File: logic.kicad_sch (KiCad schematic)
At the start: 42 parts, among them J2 TC2030, J5 Conn_01x04_Pin, J8 Conn_01x04, J9 Conn_01x04, SW1 SW_Push, SW2 SW_Push, U2 SN65HVD230, U4 HT753-1, U6 STM32F103C8Tx, Y1 8M

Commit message: schem: run and fix ERC
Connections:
- net GND: now also C6.2, C8.2, C9.2, R7.1
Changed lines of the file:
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@@
+	)
+	(symbol
+		(lib_id "power:GND")
+		(at 96.52 85.09 0)
+		(unit 1)
+		(body_style 1)
+		(exclude_from_sim no)
+		(in_bom yes)
+		(on_board yes)
+		(in_pos_files yes)
+		(dnp no)
+		(fields_autoplaced yes)
+		(property "Reference" "#PWR035"
+			(at 96.52 91.44 0)
+			(hide yes)
+			(show_name no)
+			(do_not_autoplace no)
+			(effects
+				(font
+					(size 1.27 1.27)
+				)
+			)
+		)
+		(property "Value" "GND"
+			(at 96.52 90.17 0)
+			(hide yes)
+			(show_name no)
+			(do_not_autoplace no)
+			(effects
+				(font
+					(size 1.27 1.27)
+				)
+			)
+		)
+		(property "Footprint" ""
+			(at 96.52 85.09 0)
+			(hide yes)
+			(show_name no)
+			(do_not_autoplace no)
+			(effects
+				(font
+					(size 1.27 1.27)
+				)
+			)
+		)
+		(property "Datasheet" ""
+			(at 96.52 85.09 0)
+			(hide yes)
+			(show_name no)
+			(do_not_autoplace no)
+			(effects
+				(font
+					(size 1.27 1.27)
+				)
+			)
+		)
+		(property "Description" "Power symbol creates a global label with name \"GND\" , ground"
+			(at 96.52 85.09 0)
+			(hide yes)
+			(show_name no)
+			(do_not_autoplace no)
+			(effects
+				(font
+					(size 1.27 1.27)
+				)
+			)
+		)
+		(pin "1"
+		)
+		(instances
+			(project "s6tm-detect-psu-1"
+				(path "/c28e80f1-f767-484a-bf96-16c1e8738b05/a8ebaca3-da9e-4a0a-a7e6-414b19783be9"
+					(reference "#PWR035")
+					(unit 1)
+				)
+			)
+		)
 	)
 	(symbol

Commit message: schem: add missing parts to BOM
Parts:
- J8, J9: now in the parts list
- JP4, JP5: now left out of the parts list
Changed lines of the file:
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@@
 		(body_style 1)
 		(exclude_from_sim no)
-		(in_bom no)
+		(in_bom yes)
 		(on_board yes)
 		(in_pos_files yes)
@@
 		(body_style 1)
 		(exclude_from_sim no)
-		(in_bom no)
+		(in_bom yes)
 		(on_board yes)
 		(in_pos_files yes)
@@
 		(body_style 1)
 		(exclude_from_sim no)
-		(in_bom yes)
+		(in_bom no)
 		(on_board yes)
 		(in_pos_files yes)
@@
 		(body_style 1)
 		(exclude_from_sim no)
-		(in_bom yes)
+		(in_bom no)
 		(on_board yes)
 		(in_pos_files yes)

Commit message: schem: renummber
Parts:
- renumbered C1 to C24, C2 to C25, C7 to C26, C5 to C27, C6 to C28, C8 to C29, C9 to C30, C10 to C31, C11 to C32, C12 to C33, C14 to C34, C15 to C35, C16 to C36, C38 to C37, D18 to D10, D7 to D11, D1 to D12, D2 to D13, D3 to D14, D22 to D15, D4 to D16, D5 to D17, D17 to D9, J8 to J4, J9 to J5, J5 to J6, J2 to J7, JP1 to JP3, JP5 to JP4, JP4 to JP5, R5 to R25, R7 to R26, R8 to R27, R10 to R28, TP5 to TP8, U2 to U6, U4 to U7, U6 to U8

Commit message: pcb: add can layout
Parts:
- removed D9: SMBJ6.0CA, Diode_SMD:D_SMA, symbol Device:D_TVS
- JP3: footprint Jumper:SolderJumper-2_P1.3mm_Open_RoundedPad1.0x1.5mm -> Connector_PinHeader_2.54mm:PinHeader_1x02_P2.54mm_Vertical
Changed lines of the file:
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@@
 	)
 	(junction
-		(at 83.82 181.61)
-		(diameter 0)
-		(color 0 0 0 0)
-	)
-	(junction
 		(at 125.73 40.64)
 		(diameter 0)
@@
 	(wire
 		(pts
-			(xy 83.82 182.88) (xy 83.82 181.61)
-		)
-		(stroke
-			(width 0)
-			(type default)
-		)
-	)
-	(wire
-		(pts
 			(xy 234.95 129.54) (xy 234.95 130.81)
 		)
@@
 	)
 	(symbol
-		(lib_id "Device:D_TVS")
-		(at 83.82 186.69 90)
-		(mirror x)
-		(unit 1)
-		(body_style 1)
-		(exclude_from_sim no)
-		(in_bom yes)
-		(on_board yes)
-		(in_pos_files yes)
-		(dnp no)
-		(fields_autoplaced yes)
-		(property "Reference" "D9"
-			(at 86.36 186.6899 90)
-			(show_name no)
-			(do_not_autoplace no)
-			(effects
-				(font
-					(size 1.27 1.27)
-				)
-				(justify right)
-			)
-		)
-		(property "Value" "SMBJ6.0CA"
-			(at 86.36 187.9599 90)
-			(hide yes)
-			(show_name no)
-			(do_not_autoplace no)
-			(effects
-				(font
-					(size 1.27 1.27)
-				)
-				(justify right)
-			)
-		)
-		(property "Footprint" "Diode_SMD:D_SMA"
-			(at 83.82 186.69 0)
-			(hide yes)
-			(show_name no)
-			(do_not_autoplace no)
-			(effects
-				(font
-					(size 1.27 1.27)
-				)
-			)
-		)
-		(property "Datasheet" ""
-			(at 83.82 186.69 0)
-			(hide yes)
-			(show_name no)
-			(do_not_autoplace no)
-			(effects
-				(font
-					(size 1.27 1.27)
-				)
-			)
-		)
-		(property "Description" "Bidirectional transient-voltage-suppression diode"
-			(at 83.82 186.69 0)
-			(hide yes)
-			(show_name no)
-			(do_not_autoplace no)
-			(effects
-				(font
-					(size 1.27 1.27)
-				)
-			)
-		)
-		(property "Basic" "E"
-			(at 83.82 186.69 90)
-			(hide yes)
-			(show_name no)
-			(do_not_autoplace no)
-			(effects
-				(font
-					(size 1.27 1.27)
-				)
-			)
-		)
-		(property "JLCPCB Part #" "C19077544"
-			(at 83.82 186.69 90)
-			(hide yes)
-			(show_name no)
-			(do_not_autoplace no)
-			(effects
-				(font
-					(size 1.27 1.27)
-				)
-			)
-		)
-		(property "Manufacturer" "hongjiacheng"
-			(at 83.82 186.69 90)
-			(hide yes)
-			(show_name no)
-			(do_not_autoplace no)
-			(effects
-				(font
-					(size 1.27 1.27)
-				)
-			)
-		)
-		(property "Manufacturer Part Number" "SMAJ26CA"
-			(at 83.82 186.69 90)
-			(hide yes)
-			(show_name no)
-			(do_not_autoplace no)
-			(effects
-				(font
-					(size 1.27 1.27)
-				)
-			)
-		)
-		(pin "1"
-		)
-		(pin "2"
-		)
-		(instances
-			(project "s6tm-detect-psu-1"
-				(path "/c28e80f1-f767-484a-bf96-16c1e8738b05/a8ebaca3-da9e-4a0a-a7e6-414b19783be9"
-					(reference "D9")
-					(unit 1)
-				)
-			)
-		)
-	)
-	(symbol
 		(lib_id "Connector_Generic:Conn_01x04")
 		(at 93.98 166.37 90)
@@
 			)
 		)
-		(property "Footprint" "Jumper:SolderJumper-2_P1.3mm_Open_RoundedPad1.0x1.5mm"
+		(property "Footprint" "Connector_PinHeader_2.54mm:PinHeader_1x02_P2.54mm_Vertical"
 			(at 52.07 171.45 0)
 			(hide yes)
@@
 					(unit 1)
 				)
-			)
-		)
-	)
-	(symbol
-		(lib_id "power:GND")
-		(at 83.82 190.5 0)
-		(mirror y)
-		(unit 1)
-		(body_style 1)
-		(exclude_from_sim no)
-		(in_bom yes)
-		(on_board yes)
-		(in_pos_files yes)
-		(dnp no)
-		(property "Reference" "#PWR055"
-			(at 83.82 196.85 0)
-			(hide yes)
-			(show_name no)
-			(do_not_autoplace no)
-			(effects
-				(font
-					(size 1.27 1.27)
-				)
-			)
-		)
-		(property "Value" "GND"
-			(at 79.756 192.278 0)
-			(hide yes)
-			(show_name no)
-			(do_not_autoplace no)
-			(effects
-				(font
-					(size 1.27 1.27)
-				)
-			)
-		)
-		(property "Footprint" ""
-			(at 83.82 190.5 0)
-			(hide yes)
-			(show_name no)
-			(do_not_autoplace no)
-			(effects
-				(font
-					(size 1.27 1.27)
-				)
-			)
-		)
-		(property "Datasheet" ""
-			(at 83.82 190.5 0)
-			(hide yes)
-			(show_name no)
-			(do_not_autoplace no)
-			(effects
-				(font
-					(size 1.27 1.27)
-				)
-			)
-		)
-		(property "Description" "Power symbol creates a global label with name \"GND\" , ground"
-			(at 83.82 190.5 0)
-			(hide yes)
-			(show_name no)
-			(do_not_autoplace no)
-			(effects
-				(font
-					(size 1.27 1.27)
-				)
-			)
-		)
-		(pin "1"
-		)
-		(instances
-			(project "s6tm-detect-psu-1"
-				(path "/c28e80f1-f767-484a-bf96-16c1e8738b05/a8ebaca3-da9e-4a0a-a7e6-414b19783be9"
-					(reference "#PWR055")
-					(unit 1)
-				)

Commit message: pcb: add v and i routing
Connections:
- net 5_V: now also U8.14 (PA4); no longer U8.16 (PA6)
- net BATT1_V: now also U8.16 (PA6); no longer U8.14 (PA4)
- net ILM1: now also U8.19 (PB1); no longer U8.10 (PA0)
- net ILM2: now also U8.18 (PB0); no longer U8.11 (PA1)
- net ILM3: now also U8.11 (PA1); no longer U8.18 (PB0)
- net ILM4: now also U8.10 (PA0); no longer U8.19 (PB1)
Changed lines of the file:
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@@
+		)
+	)
+	(global_label "BATT1_V"
+		(shape input)
+		(at 161.29 77.47 0)
+		(fields_autoplaced yes)
+		(effects
+			(font
+				(size 1.27 1.27)
+			)
+			(justify left)
+		)
+		(property "Intersheetrefs" "${INTERSHEET_REFS}"
+			(at 171.8347 77.47 0)
+			(hide yes)
+			(show_name no)
+			(do_not_autoplace no)
+			(effects
+				(font
+					(size 1.27 1.27)
+				)
+				(justify left)
+			)
+		)
+	)
+	(global_label "ILM3"
+		(shape input)
+		(at 161.29 64.77 0)
+		(fields_autoplaced yes)
+		(effects
+			(font
+				(size 1.27 1.27)
+			)
+			(justify left)
+		)
+		(property "Intersheetrefs" "${INTERSHEET_REFS}"
+			(at 168.569 64.77 0)
+			(hide yes)
+			(show_name no)
+			(do_not_autoplace no)
+			(effects
+				(font
+					(size 1.27 1.27)
+				)
+				(justify left)
+			)
+		)
+	)
+	(global_label "ILM4"
+		(shape input)
+		(at 161.29 62.23 0)
+		(fields_autoplaced yes)
+		(effects
+			(font
+				(size 1.27 1.27)
+			)
+			(justify left)
+		)
+		(property "Intersheetrefs" "${INTERSHEET_REFS}"
+			(at 168.569 62.23 0)
+			(hide yes)
+			(show_name no)
+			(do_not_autoplace no)
+			(effects
+				(font
+					(size 1.27 1.27)
+				)
+				(justify left)
+			)
+		)
+	)
+	(global_label "ILM2"
+		(shape input)
+		(at 123.19 90.17 180)
+		(fields_autoplaced yes)
+		(effects
+			(font
+				(size 1.27 1.27)
+			)
+			(justify right)
+		)
+		(property "Intersheetrefs" "${INTERSHEET_REFS}"
+			(at 115.911 90.17 0)
+			(hide yes)
+			(show_name no)
+			(do_not_autoplace no)
+			(effects
+				(font
+					(size 1.27 1.27)
+				)
+				(justify right)
+			)
 		)
 	)
@@
 		)
 	)
-	(global_label "ILM2"
-		(shape input)
-		(at 161.29 64.77 0)
-		(fields_autoplaced yes)
-		(effects
-			(font
-				(size 1.27 1.27)
-			)
-			(justify left)
-		)
-		(property "Intersheetrefs" "${INTERSHEET_REFS}"
-			(at 168.569 64.77 0)
-			(hide yes)
-			(show_name no)
-			(do_not_autoplace no)
-			(effects
-				(font
-					(size 1.27 1.27)
-				)
-				(justify left)
-			)
-		)
-	)
-	(global_label "BATT1_V"
+	(global_label "5_V"
 		(shape input)
 		(at 161.29 72.39 0)
@@
 		)
 		(property "Intersheetrefs" "${INTERSHEET_REFS}"
-			(at 171.8347 72.39 0)
+			(at 167.5409 72.39 0)
+			(hide yes)
+			(show_name no)
+			(do_not_autoplace no)
+			(effects
+				(font
+					(size 1.27 1.27)
+				)
+				(justify left)
+			)
+		)
+	)
+	(global_label "IN1"
+		(shape input)
+		(at 161.29 82.55 0)
+		(fields_autoplaced yes)
+		(effects
+			(font
+				(size 1.27 1.27)
+			)
+			(justify left)
+		)
+		(property "Intersheetrefs" "${INTERSHEET_REFS}"
+			(at 167.42 82.55 0)
+			(hide yes)
+			(show_name no)
+			(do_not_autoplace no)
+			(effects
+				(font
+					(size 1.27 1.27)
+				)
+				(justify left)
+			)
+		)
+	)
+	(global_label "IN2"
+		(shape input)
+		(at 161.29 85.09 0)
+		(fields_autoplaced yes)
+		(effects
+			(font
+				(size 1.27 1.27)
+			)
+			(justify left)
+		)
+		(property "Intersheetrefs" "${INTERSHEET_REFS}"
+			(at 167.42 85.09 0)
 			(hide yes)
 			(show_name no)
@@
 	(global_label "ILM1"
 		(shape input)
-		(at 161.29 62.23 0)
-		(fields_autoplaced yes)
-		(effects
-			(font
-				(size 1.27 1.27)
-			)
-			(justify left)
-		)
-		(property "Intersheetrefs" "${INTERSHEET_REFS}"
-			(at 168.569 62.23 0)
-			(hide yes)
-			(show_name no)
-			(do_not_autoplace no)
-			(effects
-				(font
-					(size 1.27 1.27)
-				)
-				(justify left)
-			)
-		)
-	)
-	(global_label "IN1"
-		(shape input)
-		(at 161.29 82.55 0)
-		(fields_autoplaced yes)
-		(effects
-			(font
-				(size 1.27 1.27)
-			)
-			(justify left)
-		)
-		(property "Intersheetrefs" "${INTERSHEET_REFS}"
-			(at 167.42 82.55 0)
-			(hide yes)
-			(show_name no)
-			(do_not_autoplace no)
-			(effects
-				(font
-					(size 1.27 1.27)
-				)
-				(justify left)
-			)
-		)
-	)
-	(global_label "ILM4"
-		(shape input)
 		(at 123.19 92.71 180)
 		(fields_autoplaced yes)
@@
 			)
 		)
-	)
-	(global_label "IN2"
-		(shape input)
-		(at 161.29 85.09 0)
-		(fields_autoplaced yes)
-		(effects
-			(font
-				(size 1.27 1.27)
-			)
-			(justify left)
-		)
-		(property "Intersheetrefs" "${INTERSHEET_REFS}"
-			(at 167.42 85.09 0)
-			(hide yes)
-			(show_name no)
-			(do_not_autoplace no)
-			(effects
-				(font
-					(size 1.27 1.27)
-				)
-				(justify left)
-			)
-		)
-	)
-	(global_label "ILM3"
-		(shape input)
-		(at 123.19 90.17 180)
-		(fields_autoplaced yes)
-		(effects
-			(font
-				(size 1.27 1.27)
-			)
-			(justify right)
-		)
-		(property "Intersheetrefs" "${INTERSHEET_REFS}"
-			(at 115.911 90.17 0)
-			(hide yes)
-			(show_name no)
-			(do_not_autoplace no)
-			(effects
-				(font
-					(size 1.27 1.27)
-				)
-				(justify right)
-			)
-		)
-	)
-	(global_label "5_V"
-		(shape input)
-		(at 161.29 77.47 0)
-		(fields_autoplaced yes)
-		(effects
-			(font
-				(size 1.27 1.27)
-			)
-			(justify left)
-		)
-		(property "Intersheetrefs" "${INTERSHEET_REFS}"
-			(at 167.5409 77.47 0)
-			(hide yes)
-			(show_name no)
-			(do_not_autoplace no)
-			(effects
-				(font
-					(size 1.27 1.27)
-				)
-				(justify left)
-			)
-		)

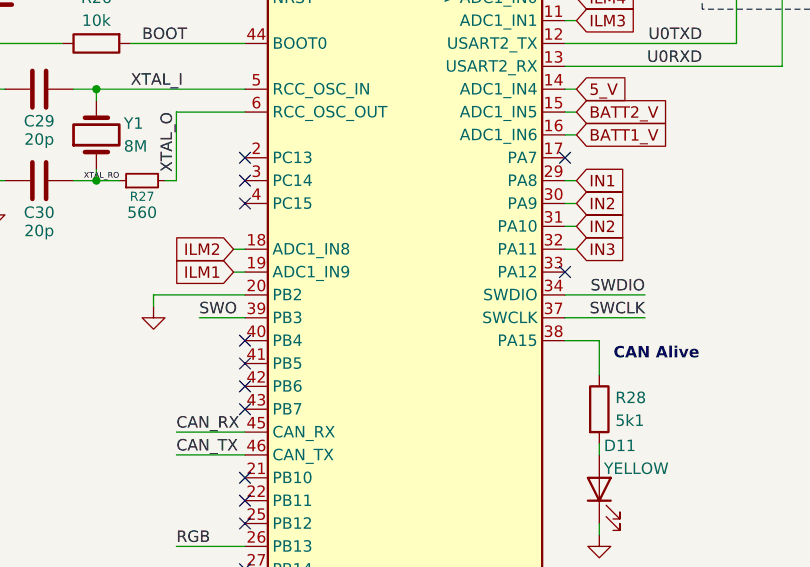
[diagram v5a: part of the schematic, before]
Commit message: pcb: route efuse signals
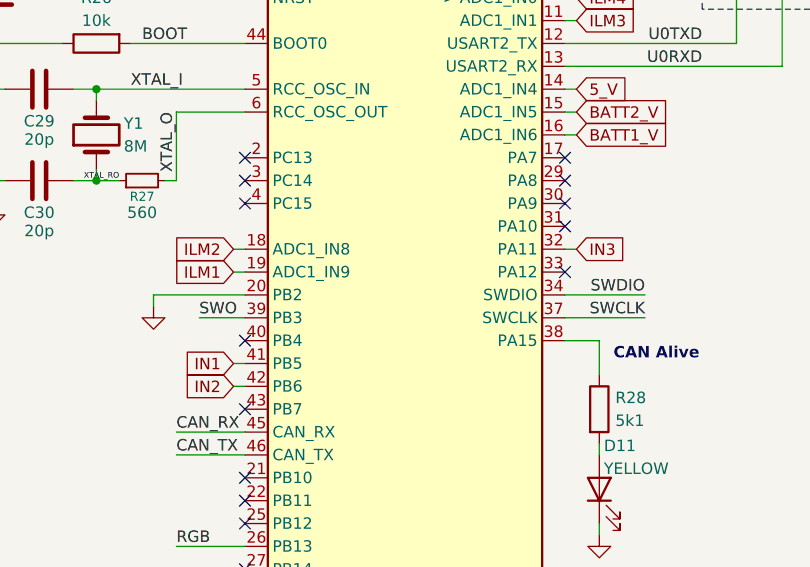
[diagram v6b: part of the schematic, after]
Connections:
- net IN1: now also U8.41 (PB5); no longer U8.29 (PA8)
- net IN2: now also U8.42 (PB6); no longer U8.30 (PA9), U8.31 (PA10)
- no-connect marks 16 -> 17
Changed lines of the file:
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@@
+	)
+	(no_connect
+		(at 160.02 85.09)
 	)
 	(no_connect
@@
 	)
 	(no_connect
-		(at 124.46 105.41)
-	)
-	(no_connect
 		(at 160.02 80.01)
 	)
@@
 	)
 	(no_connect
-		(at 124.46 102.87)
+		(at 160.02 87.63)
+	)
+	(no_connect
+		(at 160.02 82.55)
 	)
 	(no_connect
@@
 	(wire
 		(pts
-			(xy 161.29 87.63) (xy 160.02 87.63)
-		)
-		(stroke
-			(width 0)
-			(type default)
-		)
-	)
-	(wire
-		(pts
 			(xy 105.41 181.61) (xy 96.52 181.61)
 		)
@@
 	(wire
 		(pts
+			(xy 123.19 105.41) (xy 124.46 105.41)
+		)
+		(stroke
+			(width 0)
+			(type default)
+		)
+	)
+	(wire
+		(pts
 			(xy 33.02 142.24) (xy 43.18 142.24)
 		)
@@
 	(wire
 		(pts
+			(xy 123.19 102.87) (xy 124.46 102.87)
+		)
+		(stroke
+			(width 0)
+			(type default)
+		)
+	)
+	(wire
+		(pts
 			(xy 96.52 182.88) (xy 96.52 181.61)
 		)
@@
 	(wire
 		(pts
-			(xy 161.29 82.55) (xy 160.02 82.55)
-		)
-		(stroke
-			(width 0)
-			(type default)
-		)
-	)
-	(wire
-		(pts
 			(xy 250.19 157.48) (xy 250.19 158.75)
 		)
@@
 		(pts
 			(xy 245.11 144.78) (xy 256.54 144.78)
-		)
-		(stroke
-			(width 0)
-			(type default)
-		)
-	)
-	(wire
-		(pts
-			(xy 161.29 85.09) (xy 160.02 85.09)
 		)
 		(stroke
@@
 			)
 			(justify right bottom)
-		)
-	)
-	(global_label "IN2"
-		(shape input)
-		(at 161.29 87.63 0)
-		(fields_autoplaced yes)
-		(effects
-			(font
-				(size 1.27 1.27)
-			)
-			(justify left)
-		)
-		(property "Intersheetrefs" "${INTERSHEET_REFS}"
-			(at 167.42 87.63 0)
-			(hide yes)
-			(show_name no)
-			(do_not_autoplace no)
-			(effects
-				(font
-					(size 1.27 1.27)
-				)
-				(justify left)
-			)
 		)
 	)
@@
 		)
 	)
-	(global_label "ILM3"
+	(global_label "ILM2"
 		(shape input)
-		(at 161.29 64.77 0)
+		(at 123.19 90.17 180)
 		(fields_autoplaced yes)
 		(effects
@@
 				(size 1.27 1.27)
 			)
+			(justify right)
+		)
+		(property "Intersheetrefs" "${INTERSHEET_REFS}"
+			(at 115.911 90.17 0)
+			(hide yes)
+			(show_name no)
+			(do_not_autoplace no)
+			(effects
+				(font
+					(size 1.27 1.27)
+				)
+				(justify right)
+			)
+		)
+	)
+	(global_label "BATT2_V"
+		(shape input)
+		(at 161.29 74.93 0)
+		(fields_autoplaced yes)
+		(effects
+			(font
+				(size 1.27 1.27)
+			)
 			(justify left)
 		)
 		(property "Intersheetrefs" "${INTERSHEET_REFS}"
-			(at 168.569 64.77 0)
+			(at 171.8347 74.93 0)
 			(hide yes)
 			(show_name no)
@@
 				)
 				(justify left)
+			)
+		)
+	)
+	(global_label "IN3"
+		(shape input)
+		(at 161.29 90.17 0)
+		(fields_autoplaced yes)
+		(effects
+			(font
+				(size 1.27 1.27)
+			)
+			(justify left)
+		)
+		(property "Intersheetrefs" "${INTERSHEET_REFS}"
+			(at 167.42 90.17 0)
+			(hide yes)
+			(show_name no)
+			(do_not_autoplace no)
+			(effects
+				(font
+					(size 1.27 1.27)
+				)
+				(justify left)
+			)
+		)
+	)
+	(global_label "IN1"
+		(shape input)
+		(at 123.19 102.87 180)
+		(fields_autoplaced yes)
+		(effects
+			(font
+				(size 1.27 1.27)
+			)
+			(justify right)
+		)
+		(property "Intersheetrefs" "${INTERSHEET_REFS}"
+			(at 117.06 102.87 0)
+			(hide yes)
+			(show_name no)
+			(do_not_autoplace no)
+			(effects
+				(font
+					(size 1.27 1.27)
+				)
+				(justify right)
+			)
+		)
+	)
+	(global_label "5_V"
+		(shape input)
+		(at 161.29 72.39 0)
+		(fields_autoplaced yes)
+		(effects
+			(font
+				(size 1.27 1.27)
+			)
+			(justify left)
+		)
+		(property "Intersheetrefs" "${INTERSHEET_REFS}"
+			(at 167.5409 72.39 0)
+			(hide yes)
+			(show_name no)
+			(do_not_autoplace no)
+			(effects
+				(font
+					(size 1.27 1.27)
+				)
+				(justify left)
+			)
+		)
+	)
+	(global_label "IN2"
+		(shape input)
+		(at 123.19 105.41 180)
+		(fields_autoplaced yes)
+		(effects
+			(font
+				(size 1.27 1.27)
+			)
+			(justify right)
+		)
+		(property "Intersheetrefs" "${INTERSHEET_REFS}"
+			(at 117.06 105.41 0)
+			(hide yes)
+			(show_name no)
+			(do_not_autoplace no)
+			(effects
+				(font
+					(size 1.27 1.27)
+				)
+				(justify right)
 			)
 		)
@@
 		)
 	)
-	(global_label "ILM2"
+	(global_label "ILM3"
 		(shape input)
-		(at 123.19 90.17 180)
+		(at 161.29 64.77 0)
 		(fields_autoplaced yes)
 		(effects
@@
 				(size 1.27 1.27)
 			)
-			(justify right)
+			(justify left)
 		)
 		(property "Intersheetrefs" "${INTERSHEET_REFS}"
-			(at 115.911 90.17 0)
+			(at 168.569 64.77 0)
 			(hide yes)
 			(show_name no)
-			(do_not_autoplace no)
-			(effects
-				(font
-					(size 1.27 1.27)
-				)
-				(justify right)
-			)
-		)
-	)
-	(global_label "BATT2_V"
-		(shape input)
-		(at 161.29 74.93 0)
-		(fields_autoplaced yes)
-		(effects
-			(font
-				(size 1.27 1.27)
-			)
-			(justify left)
-		)
-		(property "Intersheetrefs" "${INTERSHEET_REFS}"
-			(at 171.8347 74.93 0)
-			(hide yes)
-			(show_name no)
-			(do_not_autoplace no)
-			(effects
-				(font
-					(size 1.27 1.27)
-				)
-				(justify left)
-			)
-		)
-	)
-	(global_label "IN3"
-		(shape input)
-		(at 161.29 90.17 0)
-		(fields_autoplaced yes)
-		(effects
-			(font
-				(size 1.27 1.27)
-			)
-			(justify left)
-		)
-		(property "Intersheetrefs" "${INTERSHEET_REFS}"
-			(at 167.42 90.17 0)
-			(hide yes)
-			(show_name no)
-			(do_not_autoplace no)
-			(effects
-				(font
-					(size 1.27 1.27)
-				)
-				(justify left)
-			)
-		)
-	)
-	(global_label "5_V"
-		(shape input)
-		(at 161.29 72.39 0)
-		(fields_autoplaced yes)
-		(effects
-			(font
-				(size 1.27 1.27)
-			)
-			(justify left)
-		)
-		(property "Intersheetrefs" "${INTERSHEET_REFS}"
-			(at 167.5409 72.39 0)
-			(hide yes)
-			(show_name no)
-			(do_not_autoplace no)
-			(effects
-				(font
-					(size 1.27 1.27)
-				)
-				(justify left)
-			)
-		)
-	)
-	(global_label "IN1"
-		(shape input)
-		(at 161.29 82.55 0)
-		(fields_autoplaced yes)
-		(effects
-			(font
-				(size 1.27 1.27)
-			)
-			(justify left)
-		)
-		(property "Intersheetrefs" "${INTERSHEET_REFS}"
-			(at 167.42 82.55 0)
-			(hide yes)
-			(show_name no)
-			(do_not_autoplace no)
-			(effects
-				(font
-					(size 1.27 1.27)
-				)
-				(justify left)
-			)
-		)
-	)
-	(global_label "IN2"
-		(shape input)
-		(at 161.29 85.09 0)
-		(fields_autoplaced yes)
-		(effects
-			(font
-				(size 1.27 1.27)
-			)
-			(justify left)
-		)
-		(property "Intersheetrefs" "${INTERSHEET_REFS}"
-			(at 167.42 85.09 0)
-			(hide yes)
-			(show_name no)

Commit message: pcb: route efuse gpios
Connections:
- net IN3: now also U8.2 (PC13); no longer U8.32 (PA11)
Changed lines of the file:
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@@
-	)
-	(no_connect
-		(at 124.46 80.01)
 	)
 	(no_connect
@@
 	)
 	(no_connect
+		(at 160.02 90.17)
+	)
+	(no_connect
 		(at 124.46 100.33)
 	)
@@
 		(pts
 			(xy 137.16 53.34) (xy 137.16 54.61)
-		)
-		(stroke
-			(width 0)
-			(type default)
-		)
-	)
-	(wire
-		(pts
-			(xy 161.29 90.17) (xy 160.02 90.17)
 		)
 		(stroke
@@
 		)
 	)
-	(global_label "IN3"
-		(shape input)
-		(at 161.29 90.17 0)
-		(fields_autoplaced yes)
-		(effects
-			(font
-				(size 1.27 1.27)
-			)
-			(justify left)
-		)
-		(property "Intersheetrefs" "${INTERSHEET_REFS}"
-			(at 167.42 90.17 0)
-			(hide yes)
-			(show_name no)
-			(do_not_autoplace no)
-			(effects
-				(font
-					(size 1.27 1.27)
-				)
-				(justify left)
-			)
-		)
-	)
 	(global_label "IN1"
 		(shape input)
@@
 			)
 		)
+	)
+	(global_label "IN3"
+		(shape input)
+		(at 124.46 80.01 180)
+		(fields_autoplaced yes)
+		(effects
+			(font
+				(size 1.27 1.27)
+			)
+			(justify right)
+		)
+		(property "Intersheetrefs" "${INTERSHEET_REFS}"
+			(at 118.33 80.01 0)
+			(hide yes)
+			(show_name no)
+			(do_not_autoplace no)
+			(effects
+				(font
+					(size 1.27 1.27)
+				)
+				(justify right)
+			)
+		)

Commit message: pcb: add rgb routing
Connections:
- net RGB: now also U8.17 (PA7); no longer U8.26 (PB13)
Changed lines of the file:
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@@
-	)
-	(no_connect
-		(at 160.02 80.01)
 	)
 	(no_connect
@@
 	)
 	(no_connect
+		(at 124.46 123.19)
+	)
+	(no_connect
 		(at 160.02 87.63)
 	)
@@
 	(wire
 		(pts
+			(xy 176.53 80.01) (xy 160.02 80.01)
+		)
+		(stroke
+			(width 0)
+			(type default)
+		)
+	)
+	(wire
+		(pts
 			(xy 154.94 34.29) (xy 154.94 35.56)
 		)
@@
 		(pts
 			(xy 250.19 157.48) (xy 256.54 157.48)
-		)
-		(stroke
-			(width 0)
-			(type default)
-		)
-	)
-	(wire
-		(pts
-			(xy 116.84 123.19) (xy 124.46 123.19)
 		)
 		(stroke
@@
 		)
 	)
-	(label "RGB"
-		(at 116.84 123.19 0)
-		(effects
-			(font
-				(size 1.27 1.27)
-			)
-			(justify left bottom)
-		)
-	)
 	(label "XTAL_RO"
 		(at 110.49 82.55 180)
@@
 		(effects
 			(font
+				(size 1.27 1.27)
+			)
+			(justify right bottom)
+		)
+	)
+	(label "RGB"
+		(at 176.53 80.01 180)
+		(effects
+			(font
